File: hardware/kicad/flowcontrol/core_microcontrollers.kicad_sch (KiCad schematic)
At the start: 2 parts, among them U4 XL1509-3.3

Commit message: Updated KiCad schematic to final rendition
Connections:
- net GND: now also U4.3 (FB), U4.5 (GND), U4.6 (GND), U4.7 (GND), U4.8 (GND), UC1.22 (GND), UC1.8 (GND)
- net SOL2_OUT: now reaches UC1.15 (PB1)
- net SOL1_CHECK renamed ENC_A
- net SOL1_CLOCK renamed SOL2_WAIT
- net SOL1_CONF renamed SOL2_MAIN
- net SOL1_DELAY renamed ENC_SW
- net SOL1_DURA renamed SOL2_SEL
- net SOL1_GREEN renamed SOL1_OUT
- net SOL1_RED renamed SOL1_WAIT
- net SOL2_CHECK renamed ENC_B
- net SOL2_CLOCK renamed SOL3_WAIT
- net SOL2_CONF renamed SOL3_MAIN
- net SOL2_DELAY renamed SOL3_OUT
- net SOL2_DURA renamed SOL3_SEL
- net SOL2_GREEN renamed SOL1_SEL
- net SOL2_RED renamed SOL1_MAIN
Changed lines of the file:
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@@
 	(paper "A5")
+	(junction
+		(at 76.2 110.49)
+		(diameter 0)
+		(color 0 0 0 0)
+	)
 	(junction
 		(at 76.2 22.86)
@@
 	(wire
 		(pts
+			(xy 76.2 110.49) (xy 80.01 110.49)
+		)
+		(stroke
+			(width 0)
+			(type default)
+		)
+	)
+	(wire
+		(pts
 			(xy 91.44 48.26) (xy 106.68 48.26)
 		)
@@
 	(wire
 		(pts
+			(xy 91.44 43.18) (xy 106.68 43.18)
+		)
+		(stroke
+			(width 0)
+			(type default)
+		)
+	)
+	(wire
+		(pts
 			(xy 91.44 63.5) (xy 106.68 63.5)
 		)
@@
 		)
 	)
-	(hierarchical_label "SOL1_DURA"
+	(hierarchical_label "SOL2_SEL"
 		(shape output)
 		(at 106.68 48.26 0)
@@
 		)
 	)
-	(hierarchical_label "SOL2_CLOCK"
+	(hierarchical_label "SOL3_WAIT"
 		(shape output)
 		(at 106.68 68.58 0)
@@
 		)
 	)
-	(hierarchical_label "SOL1_GREEN"
+	(hierarchical_label "SOL1_OUT"
 		(shape output)
 		(at 106.68 99.06 0)
-		(fields_autoplaced yes)
-		(effects
-			(font
-				(size 1.27 1.27)
-			)
-			(justify left)
-		)
-	)
-	(hierarchical_label "SOL1_DELAY"
-		(shape output)
-		(at 106.68 50.8 0)
 		(fields_autoplaced yes)
 		(effects
@@
 		)
 	)
-	(hierarchical_label "SOL2_RED"
+	(hierarchical_label "SOL1_MAIN"
 		(shape output)
 		(at 106.68 96.52 0)
@@
 		)
 	)
-	(hierarchical_label "SOL2_DURA"
+	(hierarchical_label "SOL3_SEL"
 		(shape output)
 		(at 106.68 71.12 0)
@@
 		)
 	)
-	(hierarchical_label "SOL1_CHECK"
+	(hierarchical_label "GND"
+		(shape output)
+		(at 80.01 110.49 0)
+		(fields_autoplaced yes)
+		(effects
+			(font
+				(size 1.27 1.27)
+			)
+			(justify left)
+		)
+	)
+	(hierarchical_label "ENC_SW"
+		(shape output)
+		(at 106.68 50.8 0)
+		(fields_autoplaced yes)
+		(effects
+			(font
+				(size 1.27 1.27)
+			)
+			(justify left)
+		)
+	)
+	(hierarchical_label "SOL2_OUT"
+		(shape output)
+		(at 106.68 43.18 0)
+		(fields_autoplaced yes)
+		(effects
+			(font
+				(size 1.27 1.27)
+			)
+			(justify left)
+		)
+	)
+	(hierarchical_label "ENC_A"
 		(shape output)
 		(at 106.68 88.9 0)
@@
 		)
 	)
-	(hierarchical_label "SOL1_CLOCK"
+	(hierarchical_label "SOL2_WAIT"
 		(shape output)
 		(at 106.68 45.72 0)
@@
 		)
 	)
-	(hierarchical_label "SOL2_CHECK"
+	(hierarchical_label "ENC_B"
 		(shape output)
 		(at 106.68 91.44 0)
@@
 		)
 	)
-	(hierarchical_label "SOL2_DELAY"
+	(hierarchical_label "SOL3_OUT"
 		(shape output)
 		(at 106.68 66.04 0)
@@
 		)
 	)
-	(hierarchical_label "SOL1_RED"
+	(hierarchical_label "SOL1_WAIT"
 		(shape output)
 		(at 106.68 93.98 0)
@@
 		)
 	)
-	(hierarchical_label "SOL2_GREEN"
+	(hierarchical_label "SOL1_SEL"
 		(shape output)
 		(at 106.68 101.6 0)
@@
 		)
 	)
-	(hierarchical_label "SOL1_CONF"
+	(hierarchical_label "SOL2_MAIN"
 		(shape output)
 		(at 106.68 40.64 0)
@@
 		)
 	)
-	(hierarchical_label "SOL2_CONF"
+	(hierarchical_label "SOL3_MAIN"
 		(shape output)
 		(at 106.68 63.5 0)

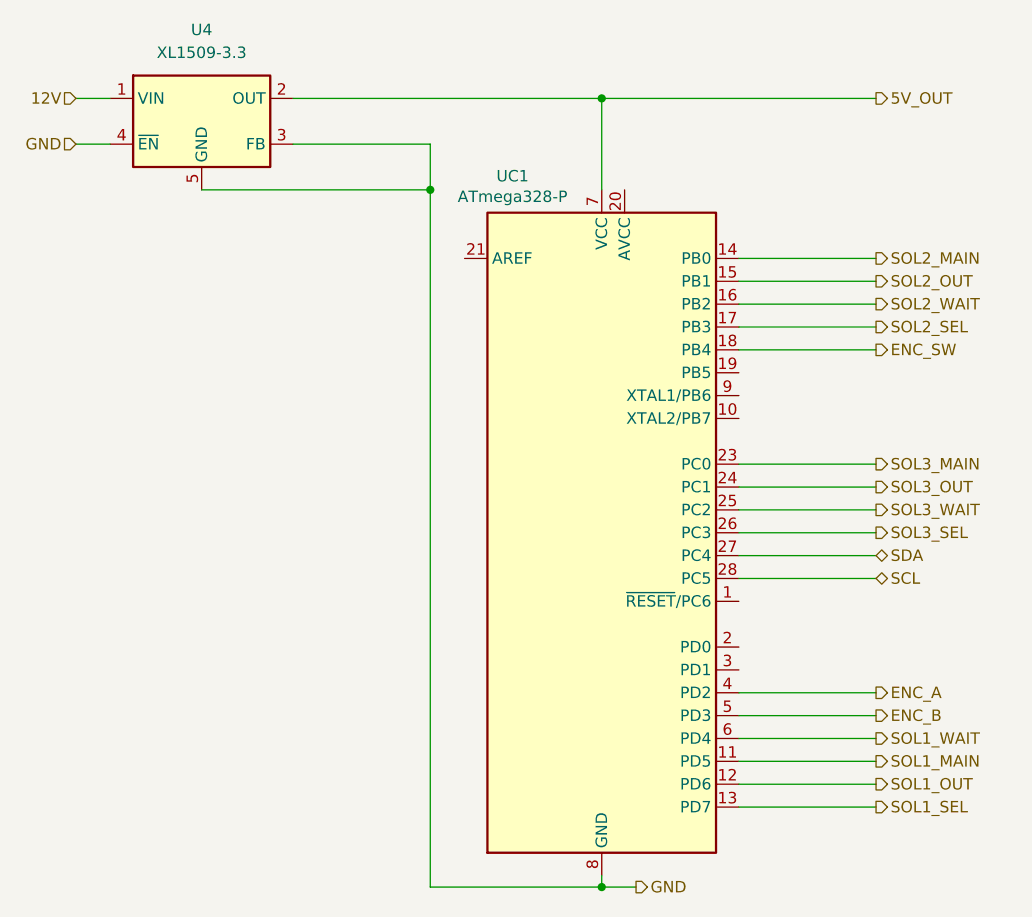
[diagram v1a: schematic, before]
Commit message: labeled the old pcb old
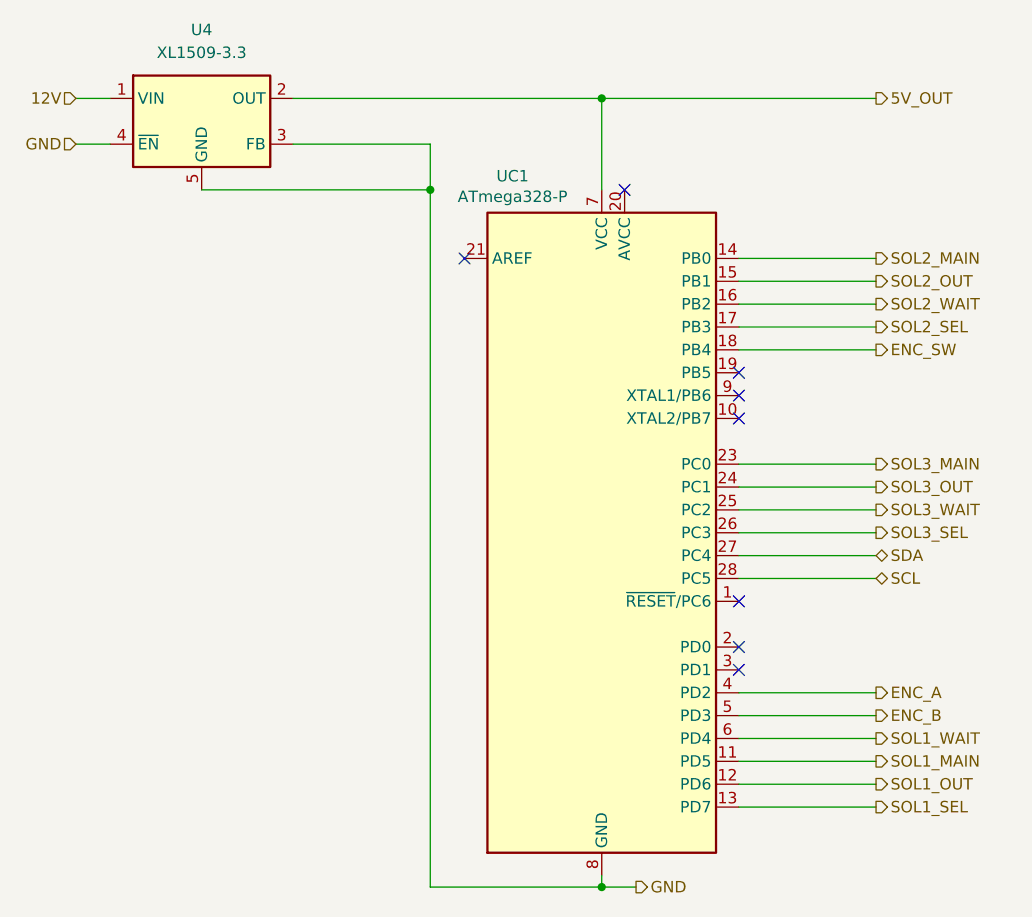
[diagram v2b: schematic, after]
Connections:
- no-connect marks 0 -> 8
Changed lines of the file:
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@@
 		(color 0 0 0 0)
+	)
+	(no_connect
+		(at 91.44 78.74)
+	)
+	(no_connect
+		(at 91.44 55.88)
+	)
+	(no_connect
+		(at 60.96 40.64)
+	)
+	(no_connect
+		(at 78.74 33.02)
+	)
+	(no_connect
+		(at 91.44 86.36)
+	)
+	(no_connect
+		(at 91.44 58.42)
+	)
+	(no_connect
+		(at 91.44 83.82)
+	)
+	(no_connect
+		(at 91.44 53.34)
 	)
 	(wire

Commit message: semi-final updates for the report
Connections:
- net 5V_OUT: now also UC1.20 (AVCC); no longer U4.2 (OUT), UC1.7 (VCC)
- new net: U4.2 (OUT), UC1.7 (VCC)
- no-connect marks 8 -> 7
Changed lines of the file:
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@@
-	)
-	(junction
-		(at 76.2 22.86)
-		(diameter 0)
-		(color 0 0 0 0)
 	)
 	(junction
@@
 	)
 	(no_connect
-		(at 78.74 33.02)
-	)
-	(no_connect
 		(at 91.44 86.36)
 	)
@@
 	(wire
 		(pts
-			(xy 76.2 22.86) (xy 106.68 22.86)
-		)
-		(stroke
-			(width 0)
-			(type default)
-		)
-	)
-	(wire
-		(pts
 			(xy 76.2 110.49) (xy 80.01 110.49)
 		)
@@
 	(wire
 		(pts
+			(xy 78.74 22.86) (xy 106.68 22.86)
+		)
+		(stroke
+			(width 0)
+			(type default)
+		)
+	)
+	(wire
+		(pts
 			(xy 91.44 63.5) (xy 106.68 63.5)
 		)
@@
 		(pts
 			(xy 41.91 27.94) (xy 57.15 27.94)
+		)
+		(stroke
+			(width 0)
+			(type default)
+		)
+	)
+	(wire
+		(pts
+			(xy 78.74 33.02) (xy 78.74 22.86)
 		)
 		(stroke
@@
 	)
 	(hierarchical_label "5V_OUT"
-		(shape output)
+		(shape input)
 		(at 106.68 22.86 0)
 		(fields_autoplaced yes)
